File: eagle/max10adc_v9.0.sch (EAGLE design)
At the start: 198 parts, among them IC1 MAX19506, IC2 MAX19506, J1 MOLEX_BNC_73100-0105, J2 MOLEX_BNC_73100-0105, J3 MOLEX_BNC_73100-0105, J4 MOLEX_BNC_73100-0105, K1 AQY21SOP, K2 AQY21SOP, K3 AQY21SOP, K4 AQY21SOP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

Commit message: v9.01
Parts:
- removed R10M_1, R10M_2, R10M_3, R10M_4: 10M, resistor:R-EU_R0805
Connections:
- removed net N$27: R10M_2.2, S2.1
- removed net N$30: R10M_3.2, S3.1
- removed net N$33: R10M_4.2, S4.1
- removed net N10M_1: R10M_1.2, S1.1
- net GND: no longer R10M_1.1, R10M_2.1, R10M_3.1, R10M_4.1
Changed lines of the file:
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@@
 <attribute name="MPN" value="SN74LVC1G3157DBV"/>
 </part>
-<part name="R10M_1" library="resistor" library_urn="urn:adsk.eagle:library:348" deviceset="R-EU_" device="R0805" package3d_urn="urn:adsk.eagle:package:26059/1" value="10M"/>
 <part name="GND9" library="supply1" deviceset="GND" device=""/>
 <part name="RIN1" library="resistor" deviceset="R-EU_" device="R0805" value="1.1M">
@@
 <attribute name="MPN" value="MF-CAP-0805-0.1uF"/>
 </part>
-<part name="R10M_3" library="resistor" library_urn="urn:adsk.eagle:library:348" deviceset="R-EU_" device="R0805" package3d_urn="urn:adsk.eagle:package:26059/1" value="10M"/>
-<part name="R10M_4" library="resistor" library_urn="urn:adsk.eagle:library:348" deviceset="R-EU_" device="R0805" package3d_urn="urn:adsk.eagle:package:26059/1" value="10M"/>
 <part name="OVSAMP1" library="74xx-little-us" deviceset="74*1G3157" device="DBVR">
 <attribute name="MPN" value="SN74LVC1G3157DBV"/>
@@
 <part name="FRAME2" library="frames" library_urn="urn:adsk.eagle:library:229" deviceset="A3L-LOC" device=""/>
 <part name="FRAME3" library="frames" library_urn="urn:adsk.eagle:library:229" deviceset="A3L-LOC" device=""/>
-<part name="R10M_2" library="resistor" library_urn="urn:adsk.eagle:library:348" deviceset="R-EU_" device="R0805" package3d_urn="urn:adsk.eagle:package:26059/1" value="10M"/>
 <part name="S1" library="switch-ck" deviceset="JS202011SCQN" device=""/>
 <part name="S2" library="switch-ck" deviceset="JS202011SCQN" device=""/>
@@
 The time constant for the AC couping is
 RC=0.01uF*10M=0.1 sec.</text>
-<text x="121.92" y="213.36" size="1.778" layer="91">These resistors, in parallel with 10M (or 50) Ohm termination,
+<text x="115.57" y="212.344" size="1.778" layer="91">These resistors, in parallel with 10M (or 50) Ohm termination,
 sets the input impedance.
 For the 1.1M case, and high impedance, it is e.g.
@@
 Variable caps are added so it can be
 adjusted in situ.</text>
+<wire x1="119.888" y1="204.216" x2="83.82" y2="231.14" width="0.254" layer="94"/>
+<wire x1="83.82" y1="228.6" x2="83.82" y2="231.14" width="0.254" layer="94"/>
+<wire x1="83.82" y1="231.14" x2="86.36" y2="231.14" width="0.254" layer="94"/>
 </plain>
 <instances>
@@
 <attribute name="VALUE" x="76.2" y="86.36" size="1.778" layer="96"/>
 </instance>
-<instance part="R10M_1" gate="G$1" x="109.22" y="210.82" rot="MR90">
-<attribute name="NAME" x="110.49" y="212.3186" size="1.778" layer="95"/>
-<attribute name="VALUE" x="110.49" y="207.518" size="1.778" layer="96"/>
-</instance>
-<instance part="GND9" gate="1" x="109.22" y="198.12" rot="MR0">
-<attribute name="VALUE" x="111.76" y="195.58" size="1.778" layer="96" rot="MR0"/>
+<instance part="GND9" gate="1" x="96.52" y="198.12" rot="MR0">
+<attribute name="VALUE" x="99.06" y="195.58" size="1.778" layer="96" rot="MR0"/>
 </instance>
 <instance part="RIN1" gate="G$1" x="109.22" y="233.68" rot="R270">
@@
 <attribute name="VALUE" x="35.56" y="231.14" size="1.778" layer="96" rot="MR0"/>
 </instance>
-<instance part="R10M_3" gate="G$1" x="299.72" y="210.82" rot="MR90">
-<attribute name="NAME" x="300.99" y="212.3186" size="1.778" layer="95"/>
-<attribute name="VALUE" x="300.99" y="207.518" size="1.778" layer="96"/>
-</instance>
-<instance part="R10M_4" gate="G$1" x="299.72" y="149.86" rot="MR90">
-<attribute name="NAME" x="300.99" y="151.3586" size="1.778" layer="95"/>
-<attribute name="VALUE" x="300.99" y="146.558" size="1.778" layer="96"/>
-</instance>
 <instance part="OVSAMP1" gate="G$1" x="109.22" y="114.3">
 <attribute name="MPN" x="104.14" y="104.14" size="1.778" layer="96" display="both"/>
@@
 <attribute name="VALUE" x="30.48" y="154.94" size="1.778" layer="96" rot="MR0"/>
 </instance>
-<instance part="GND73" gate="1" x="109.22" y="137.16" rot="MR0">
-<attribute name="VALUE" x="111.76" y="137.16" size="1.778" layer="96" rot="MR0"/>
+<instance part="GND73" gate="1" x="96.52" y="137.16" rot="MR0">
+<attribute name="VALUE" x="93.98" y="137.16" size="1.778" layer="96" rot="MR0"/>
 </instance>
 <instance part="GND74" gate="1" x="33.02" y="172.72" rot="MR0">
@@
 <attribute name="VALUE" x="215.9" y="215.9" size="1.778" layer="96"/>
 </instance>
-<instance part="GND29" gate="1" x="299.72" y="198.12" rot="MR0">
-<attribute name="VALUE" x="302.26" y="195.58" size="1.778" layer="96" rot="MR0"/>
+<instance part="GND29" gate="1" x="287.02" y="198.12" rot="MR0">
+<attribute name="VALUE" x="289.56" y="195.58" size="1.778" layer="96" rot="MR0"/>
 </instance>
 <instance part="GND35" gate="1" x="223.52" y="233.68" rot="MR0">
@@
 <attribute name="VALUE" x="215.9" y="154.94" size="1.778" layer="96"/>
 </instance>
-<instance part="GND31" gate="1" x="299.72" y="137.16" rot="MR0">
-<attribute name="VALUE" x="302.26" y="137.16" size="1.778" layer="96" rot="MR0"/>
+<instance part="GND31" gate="1" x="287.02" y="137.16" rot="MR0">
+<attribute name="VALUE" x="284.48" y="137.16" size="1.778" layer="96" rot="MR0"/>
 </instance>
 <instance part="GND56" gate="1" x="223.52" y="172.72" rot="MR0">
@@
 <attribute name="LAST_DATE_TIME" x="344.17" y="10.16" size="2.286" layer="94"/>
 <attribute name="SHEET" x="357.505" y="5.08" size="2.54" layer="94"/>
-</instance>
-<instance part="R10M_2" gate="G$1" x="109.22" y="149.86" rot="MR90">
-<attribute name="NAME" x="110.49" y="151.3586" size="1.778" layer="95"/>
-<attribute name="VALUE" x="110.49" y="146.558" size="1.778" layer="96"/>
 </instance>
 <instance part="S1" gate="G$1" x="50.8" y="220.98" rot="MR0">
@@
 </segment>
 <segment>
-<wire x1="109.22" y1="203.2" x2="96.52" y2="203.2" width="0.1524" layer="91"/>
 <pinref part="R50-4" gate="G$1" pin="2"/>
 <wire x1="96.52" y1="203.2" x2="83.82" y2="203.2" width="0.1524" layer="91"/>
@@
 <pinref part="R50-1" gate="G$1" pin="2"/>
 <wire x1="58.42" y1="205.74" x2="58.42" y2="203.2" width="0.1524" layer="91"/>
-<pinref part="R10M_1" gate="G$1" pin="1"/>
-<wire x1="109.22" y1="205.74" x2="109.22" y2="203.2" width="0.1524" layer="91"/>
 <pinref part="GND9" gate="1" pin="GND"/>
-<wire x1="109.22" y1="203.2" x2="109.22" y2="200.66" width="0.1524" layer="91"/>
-<junction x="109.22" y="203.2"/>
-</segment>
-<segment>
-<wire x1="109.22" y1="142.24" x2="109.22" y2="144.78" width="0.1524" layer="91"/>
+<wire x1="96.52" y1="203.2" x2="96.52" y2="200.66" width="0.1524" layer="91"/>
+</segment>
+<segment>
 <wire x1="58.42" y1="142.24" x2="71.12" y2="142.24" width="0.1524" layer="91"/>
 <pinref part="GND73" gate="1" pin="GND"/>
 <wire x1="71.12" y1="142.24" x2="83.82" y2="142.24" width="0.1524" layer="91"/>
 <wire x1="83.82" y1="142.24" x2="96.52" y2="142.24" width="0.1524" layer="91"/>
-<wire x1="96.52" y1="142.24" x2="109.22" y2="142.24" width="0.1524" layer="91"/>
-<wire x1="109.22" y1="139.7" x2="109.22" y2="142.24" width="0.1524" layer="91"/>
-<junction x="109.22" y="142.24"/>
+<wire x1="96.52" y1="139.7" x2="96.52" y2="142.24" width="0.1524" layer="91"/>
 <pinref part="R50-5" gate="G$1" pin="2"/>
 <wire x1="58.42" y1="144.78" x2="58.42" y2="142.24" width="0.1524" layer="91"/>
@@
 <wire x1="96.52" y1="144.78" x2="96.52" y2="142.24" width="0.1524" layer="91"/>
 <junction x="96.52" y="142.24"/>
-<pinref part="R10M_2" gate="G$1" pin="1"/>
 </segment>
 <segment>
@@
 <wire x1="287.02" y1="203.2" x2="287.02" y2="205.74" width="0.1524" layer="91"/>
 <junction x="274.32" y="203.2"/>
-<pinref part="R10M_3" gate="G$1" pin="1"/>
-<wire x1="287.02" y1="203.2" x2="299.72" y2="203.2" width="0.1524" layer="91"/>
-<wire x1="299.72" y1="203.2" x2="299.72" y2="205.74" width="0.1524" layer="91"/>
 <junction x="287.02" y="203.2"/>
 <pinref part="GND29" gate="1" pin="GND"/>
-<wire x1="299.72" y1="200.66" x2="299.72" y2="203.2" width="0.1524" layer="91"/>
-<junction x="299.72" y="203.2"/>
+<wire x1="287.02" y1="200.66" x2="287.02" y2="203.2" width="0.1524" layer="91"/>
 </segment>
 <segment>
@@
 <wire x1="287.02" y1="142.24" x2="274.32" y2="142.24" width="0.1524" layer="91"/>
 <junction x="274.32" y="142.24"/>
-<pinref part="R10M_4" gate="G$1" pin="1"/>
-<wire x1="299.72" y1="144.78" x2="299.72" y2="142.24" width="0.1524" layer="91"/>
-<wire x1="299.72" y1="142.24" x2="287.02" y2="142.24" width="0.1524" layer="91"/>
 <junction x="287.02" y="142.24"/>
 <pinref part="GND31" gate="1" pin="GND"/>
-<wire x1="299.72" y1="139.7" x2="299.72" y2="142.24" width="0.1524" layer="91"/>
-<junction x="299.72" y="142.24"/>
+<wire x1="287.02" y1="139.7" x2="287.02" y2="142.24" width="0.1524" layer="91"/>
 </segment>
 <segment>
@@
 </segment>
 </net>
-<net name="N$30" class="0">
-<segment>
-<wire x1="299.72" y1="215.9" x2="299.72" y2="223.52" width="0.1524" layer="91"/>
-<wire x1="299.72" y1="223.52" x2="246.38" y2="223.52" width="0.1524" layer="91"/>
-<pinref part="R10M_3" gate="G$1" pin="2"/>
-<pinref part="S3" gate="G$1" pin="1"/>
-</segment>
-</net>
 <net name="INA12" class="0">
 <segment>
@@
 </segment>
 </net>
-<net name="N$27" class="0">
-<segment>
-<wire x1="109.22" y1="154.94" x2="109.22" y2="162.56" width="0.1524" layer="91"/>
-<wire x1="109.22" y1="162.56" x2="55.88" y2="162.56" width="0.1524" layer="91"/>
-<pinref part="R10M_2" gate="G$1" pin="2"/>
-<pinref part="S2" gate="G$1" pin="1"/>
-</segment>
-</net>
 <net name="N$25" class="3">
 <segment>
@@
 </segment>
 </net>
-<net name="N10M_1" class="0">
-<segment>
-<pinref part="R10M_1" gate="G$1" pin="2"/>
-<wire x1="55.88" y1="223.52" x2="109.22" y2="223.52" width="0.1524" layer="91"/>
-<wire x1="109.22" y1="223.52" x2="109.22" y2="215.9" width="0.1524" layer="91"/>
-<pinref part="S1" gate="G$1" pin="1"/>
-<label x="86.36" y="223.52" size="1.778" layer="95"/>
-</segment>
-</net>
 <net name="N$26" class="3">
 <segment>
@@
 </segment>
 </net>
-<net name="N$33" class="0">
-<segment>
-<pinref part="R10M_4" gate="G$1" pin="2"/>
-<wire x1="246.38" y1="162.56" x2="299.72" y2="162.56" width="0.1524" layer="91"/>
-<wire x1="299.72" y1="162.56" x2="299.72" y2="154.94" width="0.1524" layer="91"/>
-<pinref part="S4" gate="G$1" pin="1"/>
-</segment>
-</net>

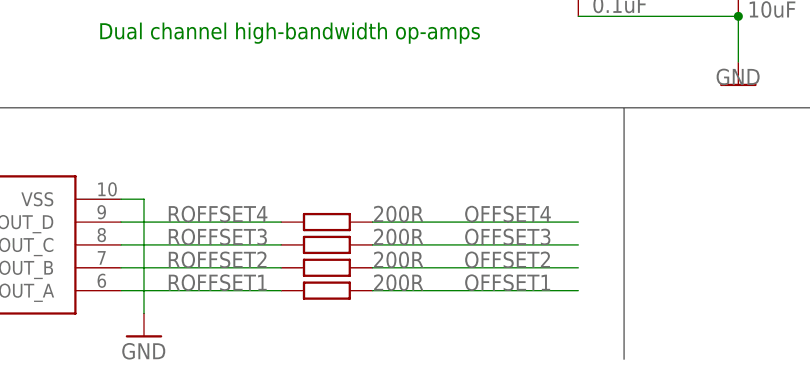
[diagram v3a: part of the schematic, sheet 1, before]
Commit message: names on silkscreen
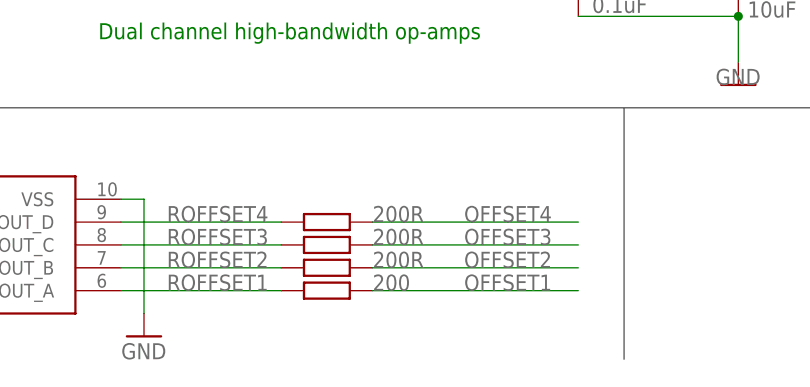
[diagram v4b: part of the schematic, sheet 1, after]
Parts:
- ROFFSET1: value 200R -> 200
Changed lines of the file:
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@@
 <attribute name="MPN" value="MF-CAP-0805-1uF"/>
 </part>
-<part name="ROFFSET1" library="resistor" library_urn="urn:adsk.eagle:library:348" deviceset="R-EU_" device="R0805" package3d_urn="urn:adsk.eagle:package:26059/1" value="200R"/>
+<part name="ROFFSET1" library="resistor" library_urn="urn:adsk.eagle:library:348" deviceset="R-EU_" device="R0805" package3d_urn="urn:adsk.eagle:package:26059/1" value="200"/>
 <part name="ROFFSET2" library="resistor" library_urn="urn:adsk.eagle:library:348" deviceset="R-EU_" device="R0805" package3d_urn="urn:adsk.eagle:package:26059/1" value="200R"/>
 <part name="ROFFSET3" library="resistor" library_urn="urn:adsk.eagle:library:348" deviceset="R-EU_" device="R0805" package3d_urn="urn:adsk.eagle:package:26059/1" value="200R"/>
